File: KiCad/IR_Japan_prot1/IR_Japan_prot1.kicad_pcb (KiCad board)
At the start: 2 copper layers, 100 x 100 mm, 64 parts, among them J1 Conn_01x09_Socket, J2 Conn_01x03_Socket, J3 Conn_01x03_Socket, J4 Conn_01x03_Socket, J5 Conn_01x03_Socket, J6 Conn_01x04_Socket, J7 Conn_01x04_Socket, J8 Conn_01x04_Socket, J9 Conn_01x03_Socket, SW1 SW_DPST_x2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

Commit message: IR完成
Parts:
- added G***: LOGO, JLCPCB_Logos:JCLPCB_30mm, F.Cu at (70.4, 109.9)
- added J10: Conn_02x03_Top_Bottom, Connector_PinHeader_2.54mm:PinHeader_2x03_P2.54mm_Vertical, F.Cu at (70.9, 91.9)
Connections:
- J4 pad 1: unconnected-(J4-Pin_1-Pad1) -> 3v3
- U17 pad 24: unconnected-(U17-*2-Pad24) -> Net-(J10-Pin_6)
- U17 pad 25: unconnected-(U17-*0-Pad25) -> Net-(J10-Pin_4)
- U17 pad 26: unconnected-(U17-*4-Pad26) -> Net-(J10-Pin_5)
- U17 pad 29: unconnected-(U17-*5,CS-Pad29) -> Net-(J10-Pin_3)
- U17 pad 32: unconnected-(U17-GND-Pad32) -> Net-(J10-Pin_1)
- U17 pad 33: unconnected-(U17-21,SDA-Pad33) -> Net-(J10-Pin_2)
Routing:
- net RX: track 0.00 -> 73.2 mm, vias 0 -> 2
- net TX: track 0.00 -> 71.3 mm, vias 0 -> 2
- net GND: track 379.1 -> 407.3 mm, vias 10 -> 12
- net Net-(J10-Pin_2): track 0.00 -> 18.9 mm
- net Net-(J10-Pin_1): track 0.00 -> 13.5 mm
- net Net-(J10-Pin_4): track 0.00 -> 10.4 mm
- net Net-(J10-Pin_6): track 0.00 -> 9.41 mm
- net 3v3: track 137.5 -> 128.3 mm
- net Net-(J10-Pin_3): track 0.00 -> 8.38 mm
- net Net-(SW1A-B): track 154.2 -> 148.3 mm
- net Net-(J10-Pin_5): track 0.00 -> 5.70 mm
- net S3: track 86.5 -> 80.8 mm
- net S2: track 87.6 -> 82.4 mm
- net Net-(U18-I15): track 51.6 -> 46.7 mm
- net IR_COM: track 17.8 -> 14.8 mm
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- added copper zone on B.Cu, net GND
- added copper zone on F.Cu, net GND
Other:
- board text added: "2/0/21"
- board text added: "2025-2026"
- board text added: "4/5/GND"
- board text added: "URAWA BEOLSAE"

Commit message: IRあと文字
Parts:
- removed J10: Conn_02x03_Top_Bottom, Connector_PinHeader_2.54mm:PinHeader_2x03_P2.54mm_Vertical
- added C17: C, Capacitor_SMD:C_0603_1608Metric_Pad1.08x0.95mm_HandSolder, F.Cu at (104.7, 70.0)
- added C18: C_Polarized_US, Capacitor_THT:C_Radial_D8.0mm_H11.5mm_P3.50mm, F.Cu at (102.9, 65.4)
- added D1: D_Schottky, Diode_SMD:D_SOD-323_HandSoldering, F.Cu at (108.1, 64.5)
- added J11: Conn_02x05_Top_Bottom, Connector_PinHeader_2.54mm:PinHeader_2x05_P2.54mm_Vertical, F.Cu at (70.4, 94.2)
- U1 /ch8: renamed from U1
- U10 /ch15: renamed from U10
- U11 /ch14: renamed from U11
- U12 /ch13: renamed from U12
- U13 /ch12: renamed from U13
- U14 /ch11: renamed from U14
- U15 /ch10: renamed from U15
- U16 /ch9: renamed from U16
- U2 /ch7: renamed from U2
- U3 /ch6: renamed from U3
- U4 /ch5: renamed from U4
- U5 /ch4: renamed from U5
- U6 /ch3: renamed from U6
- U7 /ch2: renamed from U7
- U8 /ch1: renamed from U8
- U9 /ch0: renamed from U9
- moved G*** 1.40 mm to (70.8, 111.2)
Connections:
- U17 pad 10: unconnected-(U17-26,DAC_2-Pad10) -> Net-(J11-Pin_6)
- U17 pad 12: unconnected-(U17-*14-Pad12) -> Net-(J11-Pin_4)
- U17 pad 19: VCC -> Net-(D1-K)
- U17 pad 32: Net-(J10-Pin_1) -> unconnected-(U17-GND-Pad32)
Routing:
- net Net-(D1-K): track 0.00 -> 112.5 mm, vias 0 -> 2
- net Net-(J11-Pin_6): track 0.00 -> 88.9 mm, vias 0 -> 2
- net Net-(J11-Pin_4): track 0.00 -> 87.8 mm, vias 0 -> 2
- net 3v3: track 128.3 -> 193.4 mm
- net GND: track 407.3 -> 441.6 mm, vias 12 -> 123
- net Net-(J10-Pin_1): track 13.5 -> 0.00 mm
- net TX: track 71.3 -> 84.3 mm, vias 2 -> 4
- net RX: track 73.2 -> 84.8 mm, vias 2 -> 4
- net VCC: track 36.2 -> 31.1 mm
- net Net-(SW1A-B): track 148.3 -> 144.2 mm
- net Net-(J11-Pin_8): track 9.41 -> 13.5 mm
- net Net-(U18-I6): track 49.2 -> 52.9 mm
- net Net-(U18-I7): track 53.5 -> 57.3 mm
- net Net-(U18-I5): track 47.2 -> 50.4 mm
- net Net-(J11-Pin_7): track 8.38 -> 11.3 mm
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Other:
- board text added: "0 2 26 14 5V"
- board text added: "16 17 5V GND"
- board text added: "18 19 5V GND"
- board text added: "4 5 3v3 21 GND"
- board text added: "LED MUX1 S0 S1 S2 S3 MUX2 3v3 GND"
- board text added: "TX RX 5V GND"
- board text removed: "2/0/21"
- board text removed: "4/5/GND"

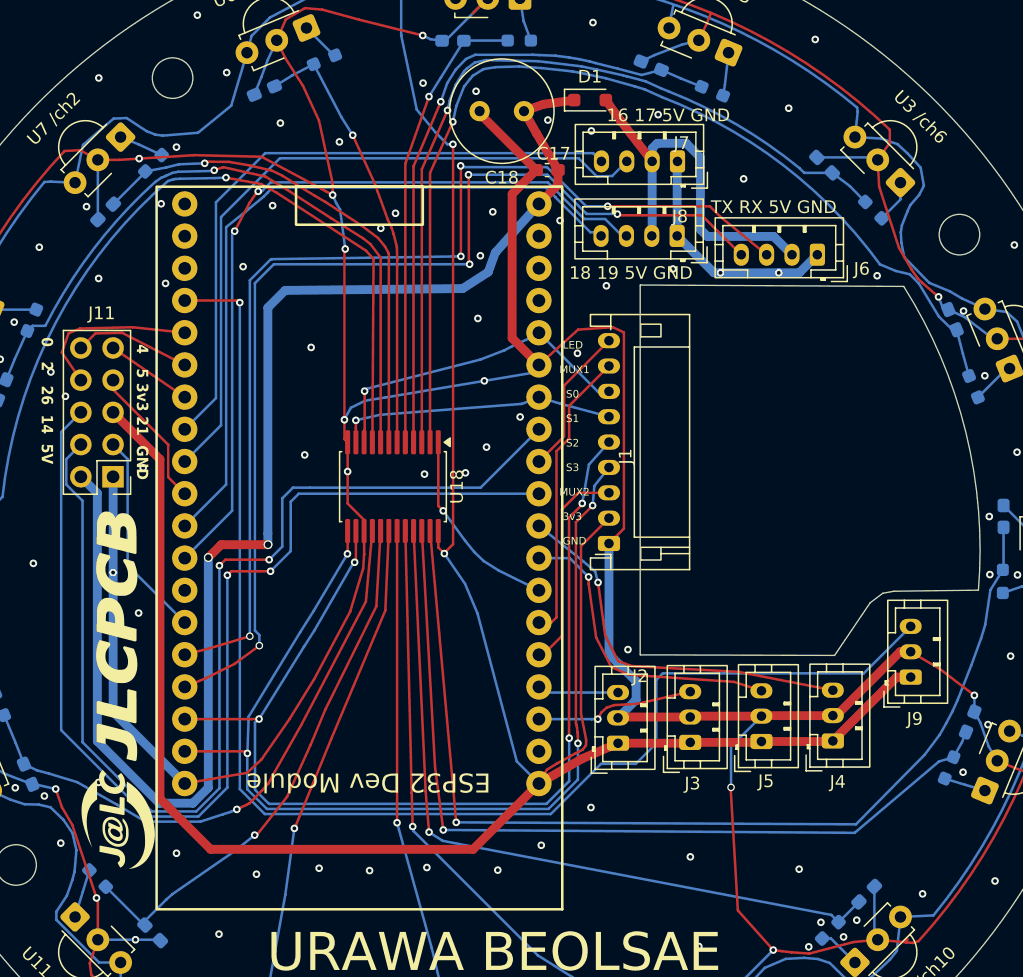
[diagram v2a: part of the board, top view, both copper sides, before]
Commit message: IRシルク書き込みまで完成
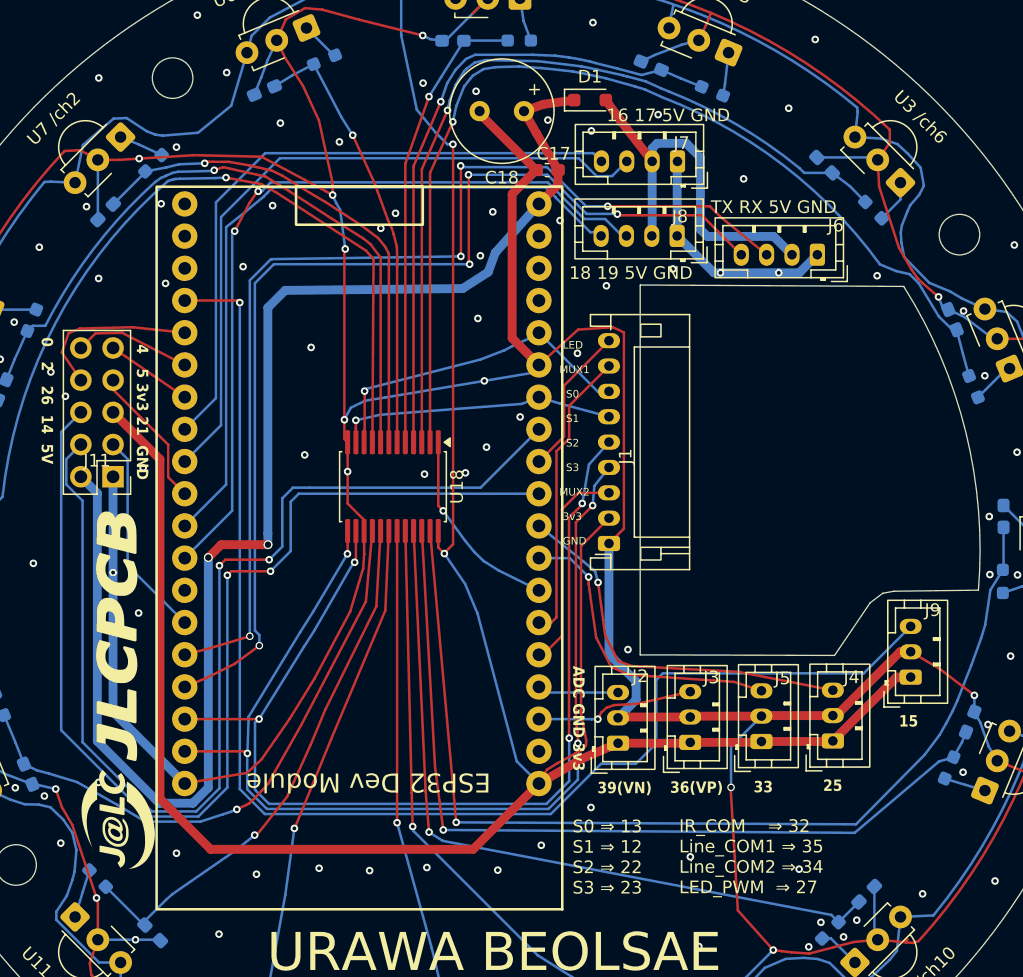
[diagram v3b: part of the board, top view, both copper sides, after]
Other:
- board text added: "+"
- board text added: "15"
- board text added: "25"
- board text added: "33"
- board text added: "36(VP)"
- board text added: "39(VN)"
- board text added: "ADC GND 3v3"
- board text added: "IR_COM ⇒ 32 Line_COM1 ⇒ 35 Line_COM2 ⇒ 34 LED_PWM ⇒ 27"
- board text added: "S0 ⇒ 13 S1 ⇒ 12 S2 ⇒ 22 S3 ⇒ 23"

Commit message: IRmadeowari
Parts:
- added J10: Conn_01x02_Socket, Connector_PinHeader_2.54mm:PinHeader_1x02_P2.54mm_Vertical, F.Cu at (121.8, 70.5)
- U1: renamed from U1 /ch8
- U10: renamed from U10 /ch15
- U11: renamed from U11 /ch14
- U12: renamed from U12 /ch13
- U13: renamed from U13 /ch12
- U14: renamed from U14 /ch11
- U15: renamed from U15 /ch10
- U16: renamed from U16 /ch9
- U2: renamed from U2 /ch7
- U3: renamed from U3 /ch6
- U4: renamed from U4 /ch5
- U5: renamed from U5 /ch4
- U6: renamed from U6 /ch3
- U7: renamed from U7 /ch2
- U8: renamed from U8 /ch1
- U9: renamed from U9 /ch0
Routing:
- net VCC: track 31.1 -> 39.3 mm
- net GND: track 441.6 -> 449.6 mm, vias 123 -> 122
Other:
- board text added: "5V GND"

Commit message: IRのXH4修正、発注
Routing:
- net GND: track 449.6 -> 468.9 mm
